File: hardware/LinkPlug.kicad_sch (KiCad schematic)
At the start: 4 parts, among them J1801 2x05_Horizontal, U1801 THVD24x2

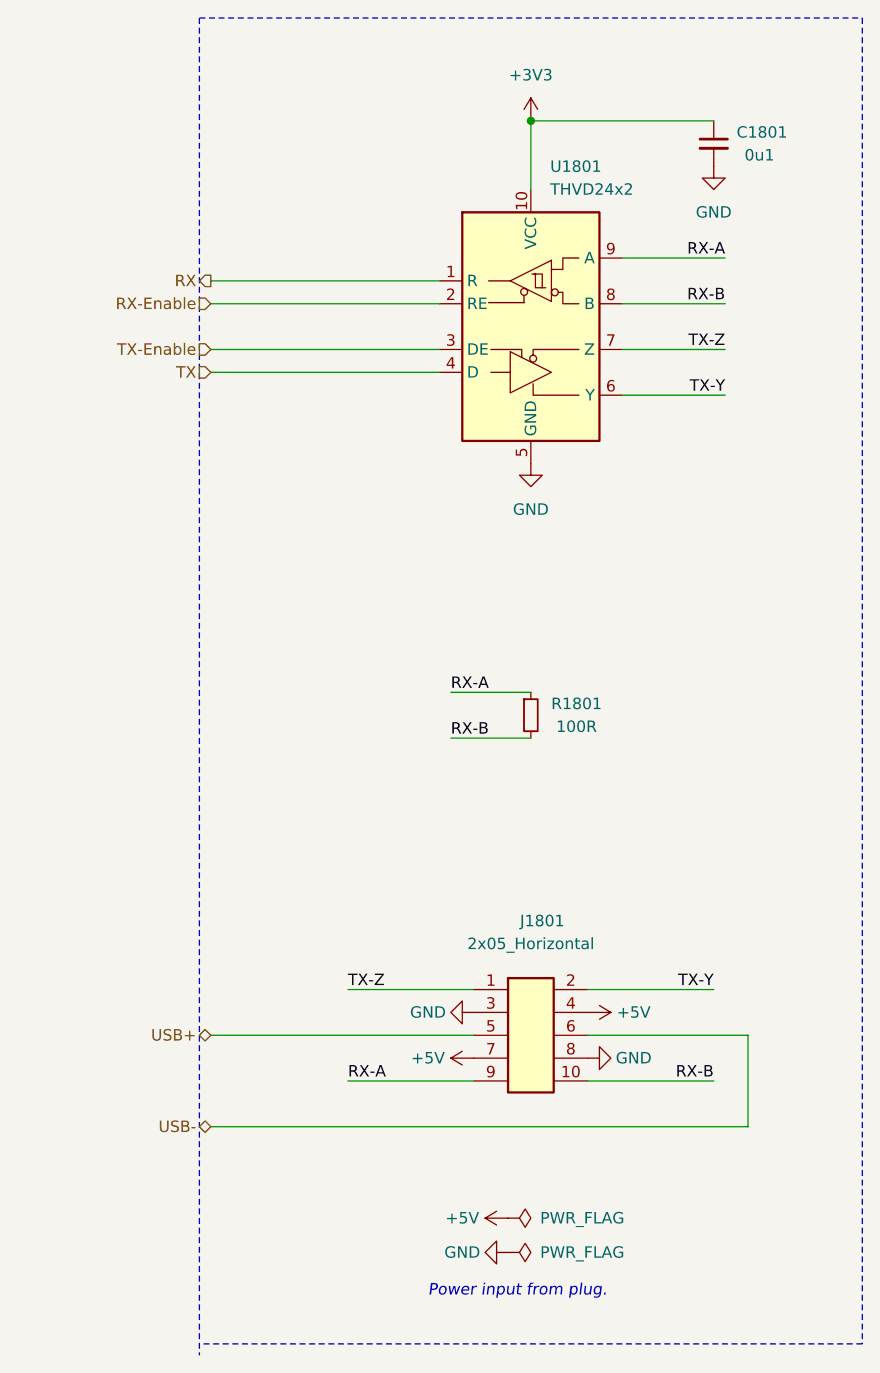
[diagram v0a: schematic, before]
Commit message: Replace Order_Number
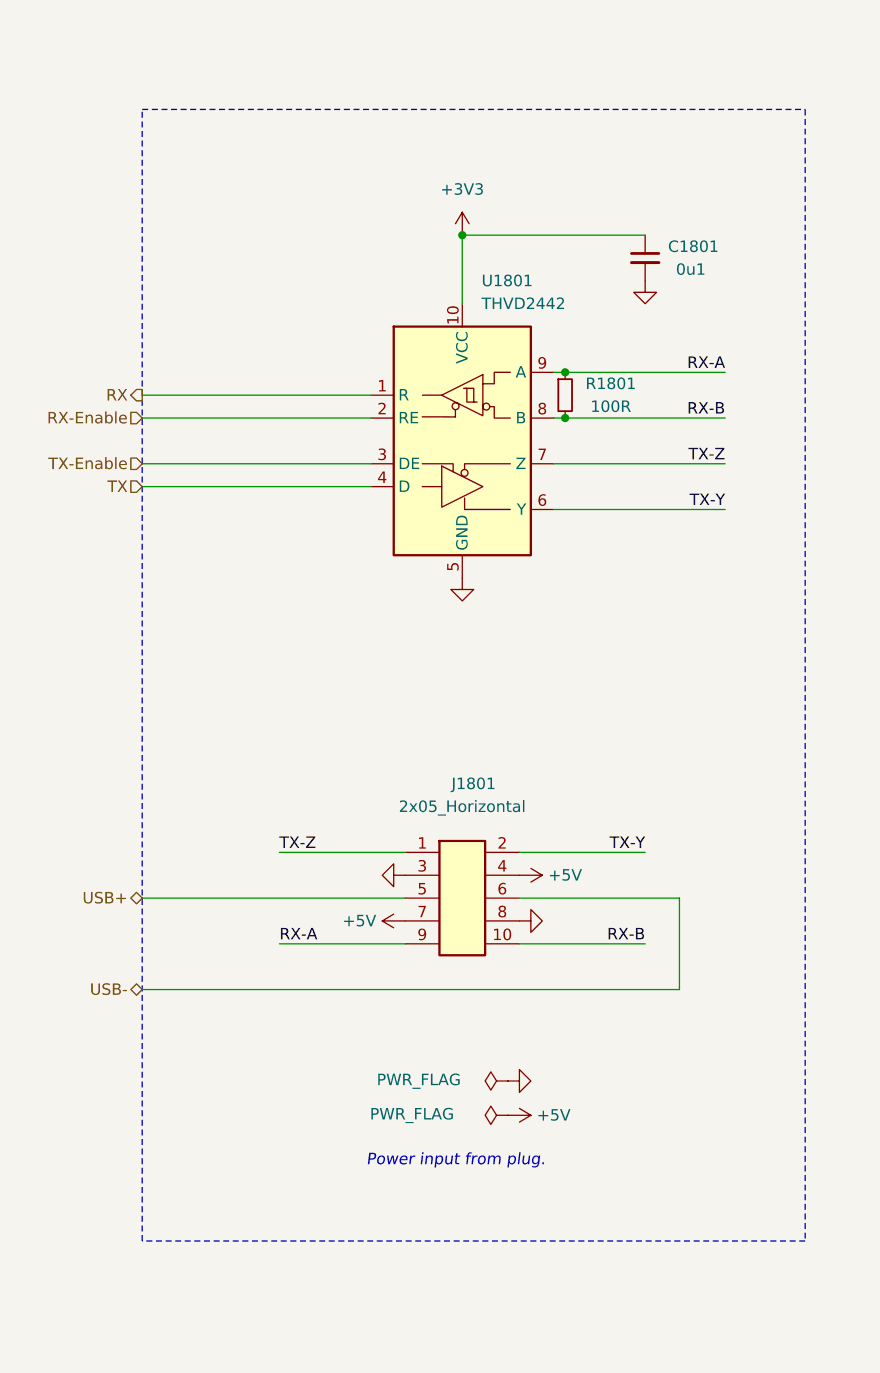
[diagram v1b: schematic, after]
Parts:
- C1801: footprint Capacitor_SMD:C_0603_1608Metric -> V2_Capacitor_SMD:C_0603; symbol Device:C_Small -> V2_Device:C_0603_0u1; Manufacturer (none) -> TDK; Mouser (none) -> 810-CGA3E2X7R1H104MA; Product (none) -> CGA3E2X7R1H104M080AA; Rating (none) -> 50V
- J1801: Manufacturer (none) -> Amphenol FCI; Mouser (none) -> 649-200211120001T4LF; Product (none) -> 20021112-00010T4LF
- R1801: footprint Resistor_SMD:R_0603_1608Metric -> V2_Resistor_SMD:R_0603; symbol Device:R_Small -> V2_Device:R_0603_100R; Manufacturer (none) -> Vishay; Mouser (none) -> 71-CRCW0603100RFKEAH; Product (none) -> CRCW0603100RFKEAHP; Rating (none) -> 330mW
- U1801: value THVD24x2 -> THVD2442; symbol V2_Interface_RS485:THVD24x2 -> V2_Interface_RS485:THVD2442; Manufacturer (none) -> Texas Instruments; Mouser (none) -> 595-THVD2442DRCR; Product (none) -> THVD2442DRCR
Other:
- moved on the sheet: C1801, J1801, R1801, U1801

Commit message: Update Library
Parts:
- C1801: symbol V2_Device:C_0603_0u1 -> V2_Capacitor:0603_0u1
- R1801: symbol V2_Device:R_0603_100R -> V2_Resistor:0603_100R
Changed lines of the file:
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@@
 		(on_board yes)
 		(dnp no)
-		(property "Reference" "#PWR01802"
+		(property "Reference" "#PWR1802"
 			(at 161.29 66.04 0)
 			(effects
@@
 			(project "express"
 				(path "/6c8448b4-b04d-47e1-934e-e40cbe27a7be/a98d6662-a9e1-4ab0-843b-cfb8511dd665"
-					(reference "#PWR01802")
+					(reference "#PWR1802")
 					(unit 1)
 				)
@@
 		(on_board yes)
 		(dnp no)
-		(property "Reference" "#FLG01802"
+		(property "Reference" "#FLG1802"
 			(at 146.05 146.685 0)
 			(effects
@@
 			(project "express"
 				(path "/6c8448b4-b04d-47e1-934e-e40cbe27a7be/a98d6662-a9e1-4ab0-843b-cfb8511dd665"
-					(reference "#FLG01802")
+					(reference "#FLG1802")
 					(unit 1)
 				)
@@
 		(on_board yes)
 		(dnp no)
-		(property "Reference" "#FLG01801"
+		(property "Reference" "#FLG1801"
 			(at 146.05 150.495 0)
 			(effects
@@
 			(project "express"
 				(path "/6c8448b4-b04d-47e1-934e-e40cbe27a7be/a98d6662-a9e1-4ab0-843b-cfb8511dd665"
-					(reference "#FLG01801")
+					(reference "#FLG1801")
 					(unit 1)
 				)
@@
 	)
 	(symbol
-		(lib_id "V2_Device:R_0603_100R")
+		(lib_id "V2_Resistor:0603_100R")
 		(at 152.4 72.39 0)
 		(unit 1)
@@
 		(on_board yes)
 		(dnp no)
-		(property "Reference" "#PWR01808"
+		(property "Reference" "#PWR1808"
 			(at 142.24 152.4 0)
 			(effects
@@
 			(project "express"
 				(path "/6c8448b4-b04d-47e1-934e-e40cbe27a7be/a98d6662-a9e1-4ab0-843b-cfb8511dd665"
-					(reference "#PWR01808")
+					(reference "#PWR1808")
 					(unit 1)
 				)
@@
 		(on_board yes)
 		(dnp no)
-		(property "Reference" "#PWR01804"
+		(property "Reference" "#PWR1804"
 			(at 128.27 125.73 0)
 			(effects
@@
 			(project "express"
 				(path "/6c8448b4-b04d-47e1-934e-e40cbe27a7be/a98d6662-a9e1-4ab0-843b-cfb8511dd665"
-					(reference "#PWR01804")
+					(reference "#PWR1804")
 					(unit 1)
 				)
@@
 		(on_board yes)
 		(dnp no)
-		(property "Reference" "#PWR01806"
+		(property "Reference" "#PWR1806"
 			(at 138.43 130.81 0)
 			(effects
@@
 			(project "express"
 				(path "/6c8448b4-b04d-47e1-934e-e40cbe27a7be/a98d6662-a9e1-4ab0-843b-cfb8511dd665"
-					(reference "#PWR01806")
+					(reference "#PWR1806")
 					(unit 1)
 				)
@@
 		(on_board yes)
 		(dnp no)
-		(property "Reference" "#PWR01803"
+		(property "Reference" "#PWR1803"
 			(at 140.97 99.06 0)
 			(effects
@@
 			(project "express"
 				(path "/6c8448b4-b04d-47e1-934e-e40cbe27a7be/a98d6662-a9e1-4ab0-843b-cfb8511dd665"
-					(reference "#PWR01803")
+					(reference "#PWR1803")
 					(unit 1)
 				)
@@
 		(on_board yes)
 		(dnp no)
-		(property "Reference" "#PWR01805"
+		(property "Reference" "#PWR1805"
 			(at 143.51 125.73 0)
 			(effects
@@
 			(project "express"
 				(path "/6c8448b4-b04d-47e1-934e-e40cbe27a7be/a98d6662-a9e1-4ab0-843b-cfb8511dd665"
-					(reference "#PWR01805")
+					(reference "#PWR1805")
 					(unit 1)
 				)
@@
 		(on_board yes)
 		(dnp no)
-		(property "Reference" "#PWR01801"
+		(property "Reference" "#PWR1801"
 			(at 140.97 58.42 0)
 			(effects
@@
 			(project "express"
 				(path "/6c8448b4-b04d-47e1-934e-e40cbe27a7be/a98d6662-a9e1-4ab0-843b-cfb8511dd665"
-					(reference "#PWR01801")
+					(reference "#PWR1801")
 					(unit 1)
 				)
@@
 		(on_board yes)
 		(dnp no)
-		(property "Reference" "#PWR01809"
+		(property "Reference" "#PWR1809"
 			(at 152.4 148.59 0)
 			(effects
@@
 			(project "express"
 				(path "/6c8448b4-b04d-47e1-934e-e40cbe27a7be/a98d6662-a9e1-4ab0-843b-cfb8511dd665"
-					(reference "#PWR01809")
+					(reference "#PWR1809")
 					(unit 1)
 				)
@@
 		(on_board yes)
 		(dnp no)
-		(property "Reference" "#PWR01807"
+		(property "Reference" "#PWR1807"
 			(at 153.67 130.81 0)
 			(effects
@@
 			(project "express"
 				(path "/6c8448b4-b04d-47e1-934e-e40cbe27a7be/a98d6662-a9e1-4ab0-843b-cfb8511dd665"
-					(reference "#PWR01807")
-					(unit 1)
-				)
-			)
-		)
-	)
-	(symbol
-		(lib_id "V2_Device:C_0603_0u1")
+					(reference "#PWR1807")
+					(unit 1)
+				)
+			)
+		)
+	)
+	(symbol
+		(lib_id "V2_Capacitor:0603_0u1")
 		(at 161.29 57.15 0)
 		(unit 1)

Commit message: Replace diode
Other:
- title: V2 Link -> V2 express

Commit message: Update
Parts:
- C1801: Id (none) -> Capacitor:${SYMBOL_NAME}
- J1801: Id (none) -> Header:${SYMBOL_NAME}
- R1801: Id (none) -> Resistor:${SYMBOL_NAME}
- U1801: Id (none) -> RS485:${SYMBOL_NAME}
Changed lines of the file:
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@@
+			)
+		)
+		(property "Id" "RS485:${SYMBOL_NAME}"
+			(at 140.97 109.22 0)
+			(hide yes)
+			(show_name no)
+			(do_not_autoplace no)
+			(effects
+				(font
+					(size 1.27 1.27)
+				)
 			)
 		)
@@
 			)
 		)
+		(property "Id" "Resistor:${SYMBOL_NAME}"
+			(at 152.4 86.36 0)
+			(hide yes)
+			(show_name no)
+			(do_not_autoplace no)
+			(effects
+				(font
+					(size 1.27 1.27)
+				)
+			)
+		)
 		(pin "1"
 		)
@@
 			)
 		)
+		(property "Id" "Header:${SYMBOL_NAME}"
+			(at 140.97 143.51 0)
+			(hide yes)
+			(show_name no)
+			(do_not_autoplace no)
+			(effects
+				(font
+					(size 1.27 1.27)
+				)
+			)
+		)
 		(pin "1"
 		)
@@
 			(hide yes)
 			(show_name no)
+			(do_not_autoplace no)
+			(effects
+				(font
+					(size 1.27 1.27)
+				)
+			)
+		)
+		(property "Id" "Capacitor:${SYMBOL_NAME}"
+			(at 161.29 72.39 0)
+			(hide yes)
+			(show_name no)

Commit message: Update
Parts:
- J1801: Rating (none) -> 1A
- U1801: Rating (none) -> 20Mbps
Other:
- company: Plug -> Versio Duo
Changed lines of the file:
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@@
 	(title_block
 		(title "V2 express")
-		(date "2026-03-30")
-		(rev "2026-03-30")
-		(company "Plug")
+		(date "2026-04-14")
+		(rev "2026-04-14")
+		(company "Versio Duo")
+		(comment 1 "Expression Controller")
 	)
 	(rectangle
@@
 		(in_pos_files yes)
 		(dnp no)
-		(property "Reference" "#PWR1802"
+		(property "Reference" "#PWR01809"
 			(at 161.29 66.04 0)
 			(hide yes)
@@
 			(project "express"
 				(path "/6c8448b4-b04d-47e1-934e-e40cbe27a7be/a98d6662-a9e1-4ab0-843b-cfb8511dd665"
-					(reference "#PWR1802")
+					(reference "#PWR01809")
 					(unit 1)
 				)
@@
 		(in_pos_files yes)
 		(dnp no)
-		(property "Reference" "#FLG1802"
+		(property "Reference" "#FLG01801"
 			(at 146.05 146.685 0)
 			(hide yes)
@@
 			(project "express"
 				(path "/6c8448b4-b04d-47e1-934e-e40cbe27a7be/a98d6662-a9e1-4ab0-843b-cfb8511dd665"
-					(reference "#FLG1802")
+					(reference "#FLG01801")
 					(unit 1)
 				)
@@
 		(in_pos_files yes)
 		(dnp no)
-		(property "Reference" "#FLG1801"
+		(property "Reference" "#FLG01802"
 			(at 146.05 150.495 0)
 			(hide yes)
@@
 			(project "express"
 				(path "/6c8448b4-b04d-47e1-934e-e40cbe27a7be/a98d6662-a9e1-4ab0-843b-cfb8511dd665"
-					(reference "#FLG1801")
+					(reference "#FLG01802")
 					(unit 1)
 				)
@@
 			)
 		)
+		(property "Rating" "20Mbps"
+			(at 142.24 116.84 0)
+			(hide yes)
+			(show_name no)
+			(do_not_autoplace no)
+			(effects
+				(font
+					(size 1.27 1.27)
+				)
+			)
+		)
 		(pin "1"
 		)
@@
 			)
 		)
+		(property "Rating" "1A"
+			(at 140.97 158.75 0)
+			(hide yes)
+			(show_name no)
+			(do_not_autoplace no)
+			(effects
+				(font
+					(size 1.27 1.27)
+				)
+			)
+		)
 		(pin "1"
 		)
@@
 		(in_pos_files yes)
 		(dnp no)
-		(property "Reference" "#PWR1808"
+		(property "Reference" "#PWR01806"
 			(at 142.24 152.4 0)
 			(hide yes)
@@
 			(project "express"
 				(path "/6c8448b4-b04d-47e1-934e-e40cbe27a7be/a98d6662-a9e1-4ab0-843b-cfb8511dd665"
-					(reference "#PWR1808")
+					(reference "#PWR01806")
 					(unit 1)
 				)
@@
 		(in_pos_files yes)
 		(dnp no)
-		(property "Reference" "#PWR1804"
+		(property "Reference" "#PWR01801"
 			(at 128.27 125.73 0)
 			(hide yes)
@@
 			(project "express"
 				(path "/6c8448b4-b04d-47e1-934e-e40cbe27a7be/a98d6662-a9e1-4ab0-843b-cfb8511dd665"
-					(reference "#PWR1804")
+					(reference "#PWR01801")
 					(unit 1)
 				)
@@
 		(in_pos_files yes)
 		(dnp no)
-		(property "Reference" "#PWR1806"
+		(property "Reference" "#PWR01802"
 			(at 138.43 130.81 0)
 			(hide yes)
@@
 			(project "express"
 				(path "/6c8448b4-b04d-47e1-934e-e40cbe27a7be/a98d6662-a9e1-4ab0-843b-cfb8511dd665"
-					(reference "#PWR1806")
+					(reference "#PWR01802")
 					(unit 1)
 				)
@@
 		(in_pos_files yes)
 		(dnp no)
-		(property "Reference" "#PWR1803"
+		(property "Reference" "#PWR01804"
 			(at 140.97 99.06 0)
 			(hide yes)
@@
 			(project "express"
 				(path "/6c8448b4-b04d-47e1-934e-e40cbe27a7be/a98d6662-a9e1-4ab0-843b-cfb8511dd665"
-					(reference "#PWR1803")
+					(reference "#PWR01804")
 					(unit 1)
 				)
@@
 		(in_pos_files yes)
 		(dnp no)
-		(property "Reference" "#PWR1805"
+		(property "Reference" "#PWR01807"
 			(at 143.51 125.73 0)
 			(hide yes)
@@
 			(project "express"
 				(path "/6c8448b4-b04d-47e1-934e-e40cbe27a7be/a98d6662-a9e1-4ab0-843b-cfb8511dd665"
-					(reference "#PWR1805")
+					(reference "#PWR01807")
 					(unit 1)
 				)
@@
 		(in_pos_files yes)
 		(dnp no)
-		(property "Reference" "#PWR1801"
+		(property "Reference" "#PWR01803"
 			(at 140.97 58.42 0)
 			(hide yes)
@@
 			(project "express"
 				(path "/6c8448b4-b04d-47e1-934e-e40cbe27a7be/a98d6662-a9e1-4ab0-843b-cfb8511dd665"
-					(reference "#PWR1801")
+					(reference "#PWR01803")
 					(unit 1)
 				)
@@
 		(in_pos_files yes)
 		(dnp no)
-		(property "Reference" "#PWR1809"
+		(property "Reference" "#PWR01805"
 			(at 152.4 148.59 0)
 			(hide yes)
@@
 			(project "express"
 				(path "/6c8448b4-b04d-47e1-934e-e40cbe27a7be/a98d6662-a9e1-4ab0-843b-cfb8511dd665"
-					(reference "#PWR1809")
+					(reference "#PWR01805")
 					(unit 1)
 				)
@@
 		(in_pos_files yes)
 		(dnp no)
-		(property "Reference" "#PWR1807"
+		(property "Reference" "#PWR01808"
 			(at 153.67 130.81 0)
 			(hide yes)
@@
 			(project "express"
 				(path "/6c8448b4-b04d-47e1-934e-e40cbe27a7be/a98d6662-a9e1-4ab0-843b-cfb8511dd665"
-					(reference "#PWR1807")
+					(reference "#PWR01808")
 					(unit 1)
 				)

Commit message: Good Bye Imperial
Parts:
- C1801: footprint V2_Capacitor_SMD:C_0603 -> V2_Capacitor_SMD:C_1608; symbol V2_Capacitor:0603_0u1 -> V2_Capacitor:1608_0u1
- R1801: footprint V2_Resistor_SMD:R_0603 -> V2_Resistor_SMD:R_1608; symbol V2_Resistor:0603_100R -> V2_Resistor:1608_100R
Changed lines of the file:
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@@
 	)
 	(symbol
-		(lib_id "V2_Resistor:0603_100R")
+		(lib_id "V2_Resistor:1608_100R")
 		(at 152.4 72.39 0)
 		(unit 1)
@@
 			)
 		)
-		(property "Footprint" "V2_Resistor_SMD:R_0603"
+		(property "Footprint" "V2_Resistor_SMD:R_1608"
 			(at 152.4 88.138 0)
 			(hide yes)
@@
 	)
 	(symbol
-		(lib_id "V2_Capacitor:0603_0u1")
+		(lib_id "V2_Capacitor:1608_0u1")
 		(at 161.29 57.15 0)
 		(unit 1)
@@
 			)
 		)
-		(property "Footprint" "V2_Capacitor_SMD:C_0603"
+		(property "Footprint" "V2_Capacitor_SMD:C_1608"
 			(at 161.29 74.168 0)
 			(hide yes)
